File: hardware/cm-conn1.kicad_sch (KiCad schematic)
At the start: 7 parts, among them J3 RJ45_RB1-125B8G1A

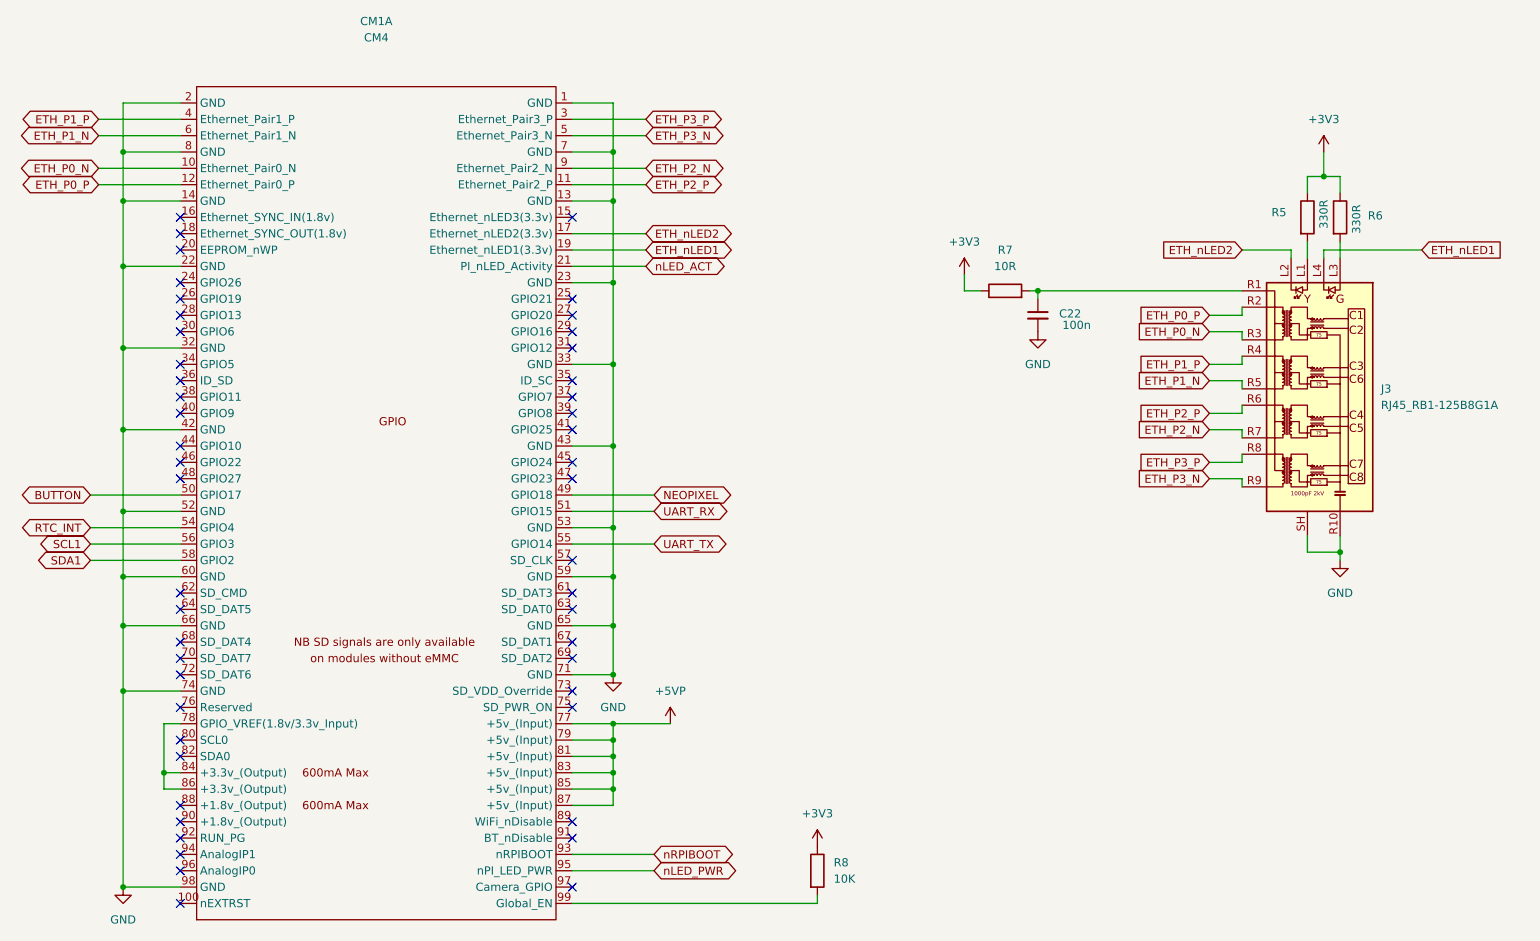
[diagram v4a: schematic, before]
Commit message: Standardize all resistors to R_Small, fix broken R22 connection
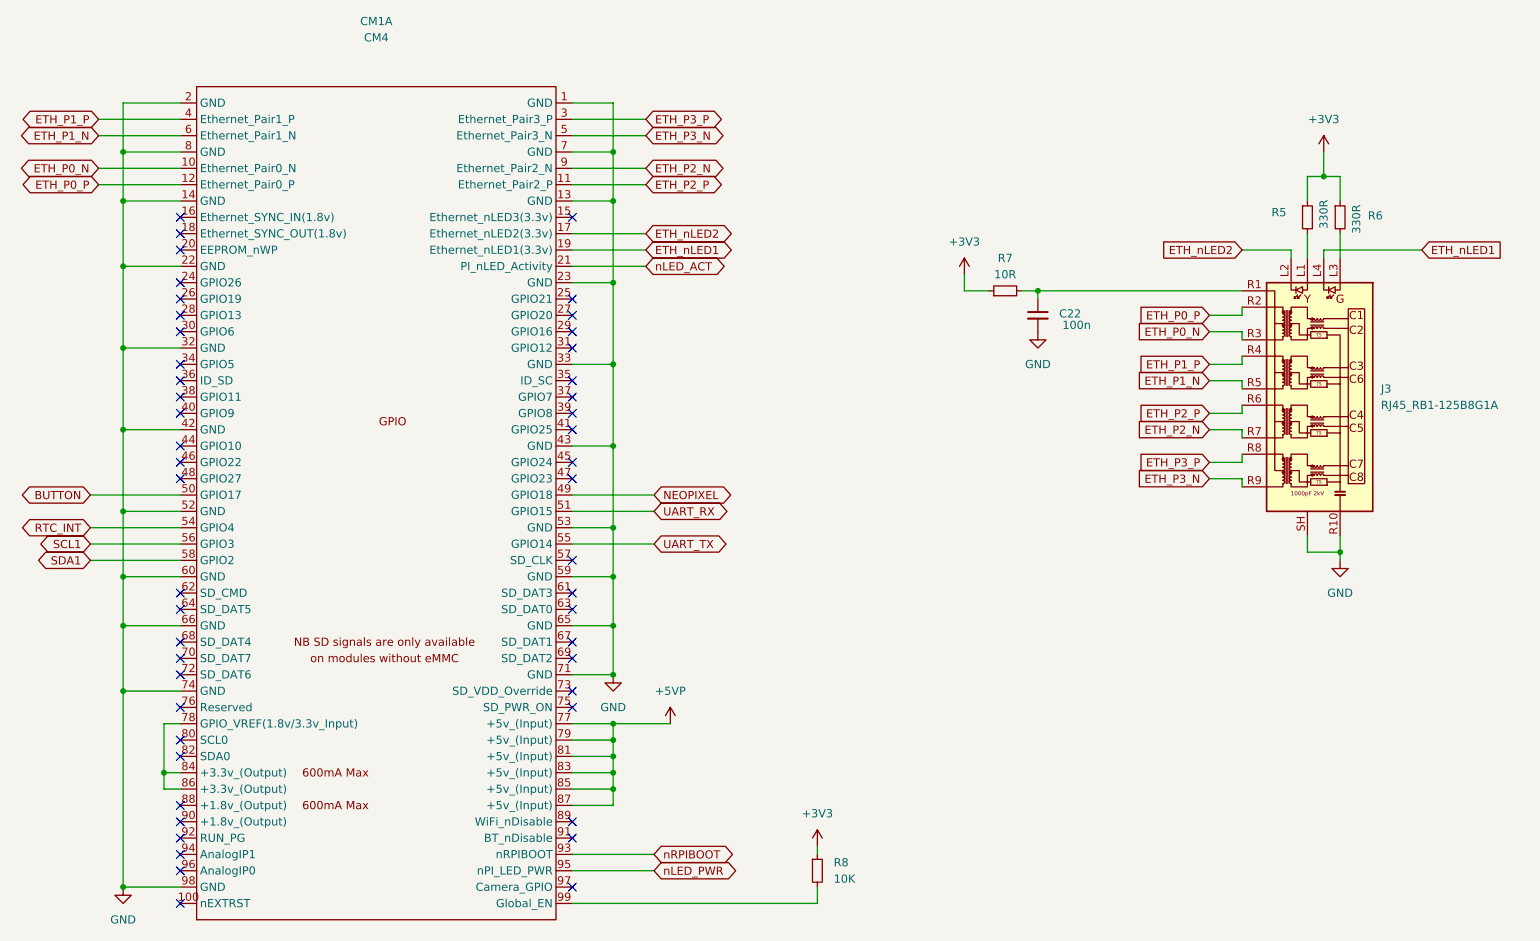
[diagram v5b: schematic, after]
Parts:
- R5, R6, R7, R8: symbol Device:R -> Device:R_Small
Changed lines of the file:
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@@
 	(wire
 		(pts
+			(xy 153.67 156.21) (xy 153.67 157.48)
+		)
+		(stroke
+			(width 0)
+			(type default)
+		)
+	)
+	(wire
+		(pts
 			(xy 229.87 110.49) (xy 234.95 110.49)
 		)
@@
 	(wire
 		(pts
-			(xy 229.87 52.07) (xy 229.87 54.61)
+			(xy 229.87 52.07) (xy 229.87 55.88)
 		)
 		(stroke
@@
 	(wire
 		(pts
-			(xy 54.61 78.74) (xy 45.72 78.74)
+			(xy 234.95 52.07) (xy 234.95 55.88)
 		)
 		(stroke
@@
 	(wire
 		(pts
-			(xy 45.72 132.08) (xy 45.72 162.56)
+			(xy 54.61 78.74) (xy 45.72 78.74)
 		)
 		(stroke
@@
 	(wire
 		(pts
-			(xy 234.95 62.23) (xy 234.95 64.77)
+			(xy 45.72 132.08) (xy 45.72 162.56)
 		)
 		(stroke
@@
 	(wire
 		(pts
+			(xy 185.42 69.85) (xy 187.96 69.85)
+		)
+		(stroke
+			(width 0)
+			(type default)
+		)
+	)
+	(wire
+		(pts
 			(xy 121.92 139.7) (xy 121.92 142.24)
 		)
@@
 	(wire
 		(pts
-			(xy 229.87 62.23) (xy 229.87 64.77)
+			(xy 229.87 60.96) (xy 229.87 64.77)
 		)
 		(stroke
@@
 	(wire
 		(pts
+			(xy 153.67 162.56) (xy 153.67 165.1)
+		)
+		(stroke
+			(width 0)
+			(type default)
+		)
+	)
+	(wire
+		(pts
 			(xy 219.71 95.25) (xy 219.71 96.52)
 		)
@@
 	(wire
 		(pts
-			(xy 54.61 40.64) (xy 45.72 40.64)
+			(xy 234.95 60.96) (xy 234.95 64.77)
 		)
 		(stroke
@@
 	(wire
 		(pts
-			(xy 234.95 54.61) (xy 234.95 52.07)
+			(xy 54.61 40.64) (xy 45.72 40.64)
 		)
 		(stroke
@@
 	(wire
 		(pts
-			(xy 176.53 69.85) (xy 179.07 69.85)
+			(xy 176.53 69.85) (xy 180.34 69.85)
 		)
 		(stroke
@@
 	(wire
 		(pts
-			(xy 186.69 69.85) (xy 187.96 69.85)
-		)
-		(stroke
-			(width 0)
-			(type default)
-		)
-	)
-	(wire
-		(pts
 			(xy 121.92 93.98) (xy 121.92 106.68)
 		)
@@
 	(wire
 		(pts
-			(xy 153.67 163.83) (xy 153.67 165.1)
-		)
-		(stroke
-			(width 0)
-			(type default)
-		)
-	)
-	(wire
-		(pts
 			(xy 121.92 149.86) (xy 121.92 147.32)
 		)
@@
 	)
 	(symbol
-		(lib_id "Device:R")
+		(lib_id "Device:R_Small")
 		(at 182.88 69.85 90)
 		(unit 1)
@@
 		(fields_autoplaced yes)
 		(property "Reference" "R7"
-			(at 182.88 63.5 90)
+			(at 182.88 64.77 90)
 			(show_name no)
 			(do_not_autoplace no)
@@
 		)
 		(property "Value" "10R"
-			(at 182.88 66.04 90)
+			(at 182.88 67.31 90)
 			(show_name no)
 			(do_not_autoplace no)
@@
 		)
 		(property "Footprint" "Resistor_SMD:R_0805_2012Metric"
-			(at 182.88 71.628 90)
+			(at 182.88 69.85 0)
 			(hide yes)
 			(show_name no)
@@
 			)
 		)
-		(property "Description" "Resistor"
+		(property "Description" "Resistor, small symbol"
 			(at 182.88 69.85 0)
 			(hide yes)
@@
 	)
 	(symbol
-		(lib_id "Device:R")
+		(lib_id "Device:R_Small")
 		(at 153.67 160.02 0)
 		(unit 1)
@@
 		)
 		(property "Footprint" "Resistor_SMD:R_0805_2012Metric"
-			(at 151.892 160.02 90)
+			(at 153.67 160.02 0)
 			(hide yes)
 			(show_name no)
@@
 			)
 		)
-		(property "Description" "Resistor"
+		(property "Description" "Resistor, small symbol"
 			(at 153.67 160.02 0)
 			(hide yes)
@@
 	)
 	(symbol
-		(lib_id "Device:R")
+		(lib_id "Device:R_Small")
 		(at 234.95 58.42 0)
 		(unit 1)
@@
 		)
 		(property "Footprint" "Resistor_SMD:R_0805_2012Metric"
-			(at 233.172 58.42 90)
+			(at 234.95 58.42 0)
 			(hide yes)
 			(show_name no)
@@
 			)
 		)
-		(property "Description" "Resistor"
+		(property "Description" "Resistor, small symbol"
 			(at 234.95 58.42 0)
 			(hide yes)
@@
 	)
 	(symbol
-		(lib_id "Device:R")
+		(lib_id "Device:R_Small")
 		(at 229.87 58.42 0)
 		(unit 1)
@@
 		)
 		(property "Footprint" "Resistor_SMD:R_0805_2012Metric"
-			(at 228.092 58.42 90)
+			(at 229.87 58.42 0)
 			(hide yes)
 			(show_name no)
@@
 			)
 		)
-		(property "Description" "Resistor"
+		(property "Description" "Resistor, small symbol"
 			(at 229.87 58.42 0)
 			(hide yes)
